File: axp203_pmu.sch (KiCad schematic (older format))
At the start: 1 part

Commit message: Updated PCB
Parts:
- U1: renamed from U?; footprint (none) -> X_Powers:AXP203_QFN48
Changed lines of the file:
@@
 $EndDescr
 $Comp
-L x_powers:AXP203 U?
+L x_powers:AXP203 U1
 U 1 1 5E09CC8E
 P 7900 5000
-F 0 "U?" H 7900 7565 50  0000 C CNN
+F 0 "U1" H 7900 7565 50  0000 C CNN
 F 1 "AXP203" H 7900 7474 50  0000 C CNN
-F 2 "" H 3550 7200 50  0001 C CNN
+F 2 "X_Powers:AXP203_QFN48" H 3550 7200 50  0001 C CNN
 F 3 "/home/mw/kicad_library/Schematic/PMU_Units/X_Powers/Components_Documentation/AXP203_Datasheet_V1.0.pdf" H 3550 7200 50  0001 C CNN
 	1    7900 5000

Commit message: Continue activity
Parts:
- removed U1: AXP203, X_Powers:AXP203_QFN48, symbol x_powers:AXP203
- added U?: AXP203, symbol x_powers:AXP203
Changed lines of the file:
@@
 $EndDescr
 $Comp
-L x_powers:AXP203 U1
-U 1 1 5E09CC8E
-P 7900 5000
-F 0 "U1" H 7900 7565 50  0000 C CNN
-F 1 "AXP203" H 7900 7474 50  0000 C CNN
-F 2 "X_Powers:AXP203_QFN48" H 3550 7200 50  0001 C CNN
-F 3 "/home/mw/kicad_library/Schematic/PMU_Units/X_Powers/Components_Documentation/AXP203_Datasheet_V1.0.pdf" H 3550 7200 50  0001 C CNN
-	1    7900 5000
+L x_powers:AXP203 U?
+U 1 1 5E04BBCA
+P 8350 5350
+F 0 "U?" H 8350 7915 50  0000 C CNN
+F 1 "AXP203" H 8350 7824 50  0000 C CNN
+F 2 "" H 4000 7550 50  0001 C CNN
+F 3 "/home/mw/kicad_library/Schematic/PMU_Units/X_Powers/Components_Documentation/AXP203_Datasheet_V1.0.pdf" H 4000 7550 50  0001 C CNN
+	1    8350 5350
 	1    0    0    -1
 $EndComp

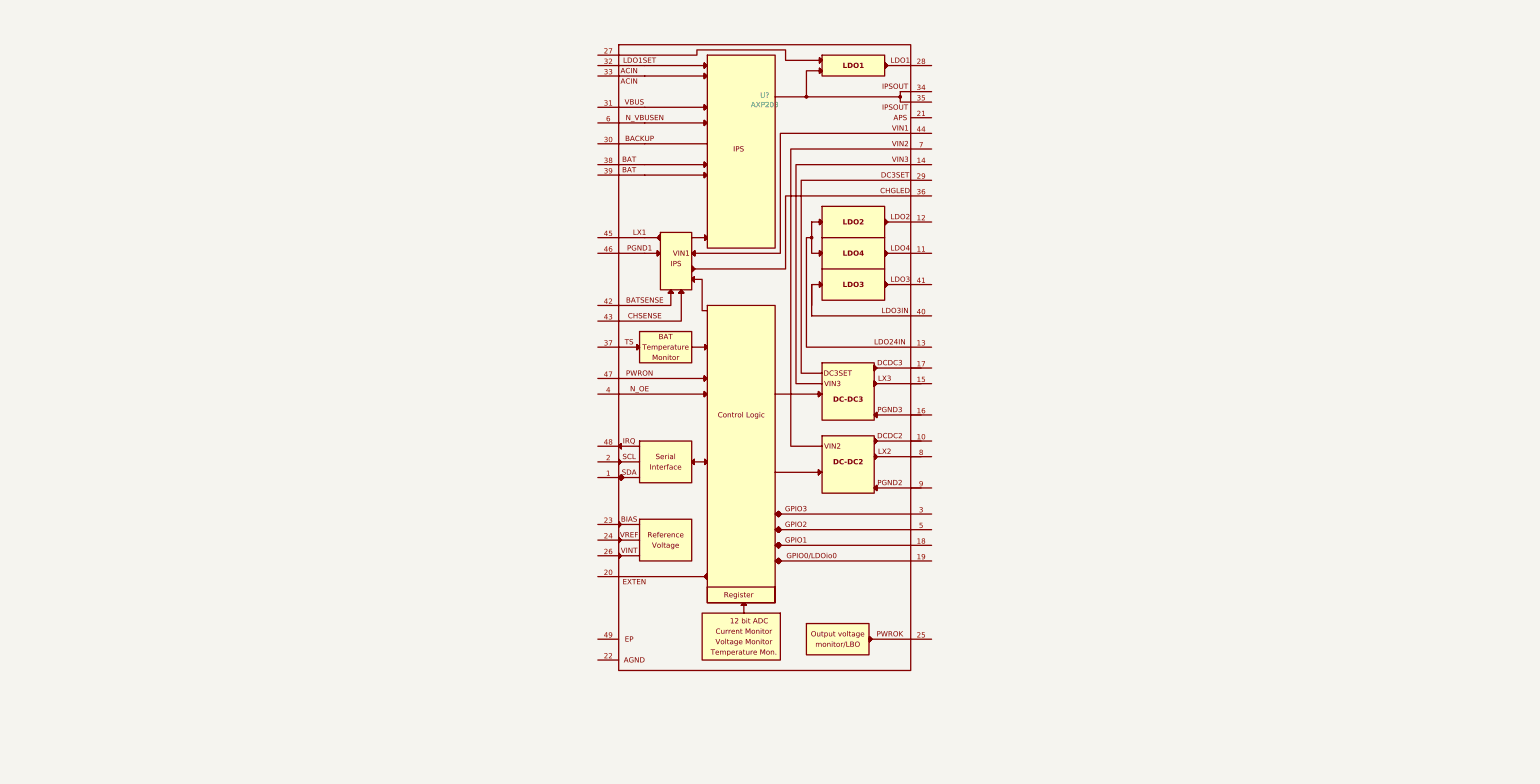
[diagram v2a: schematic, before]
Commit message: Schematic finished, pcb components added in pcb, axp schematic checked
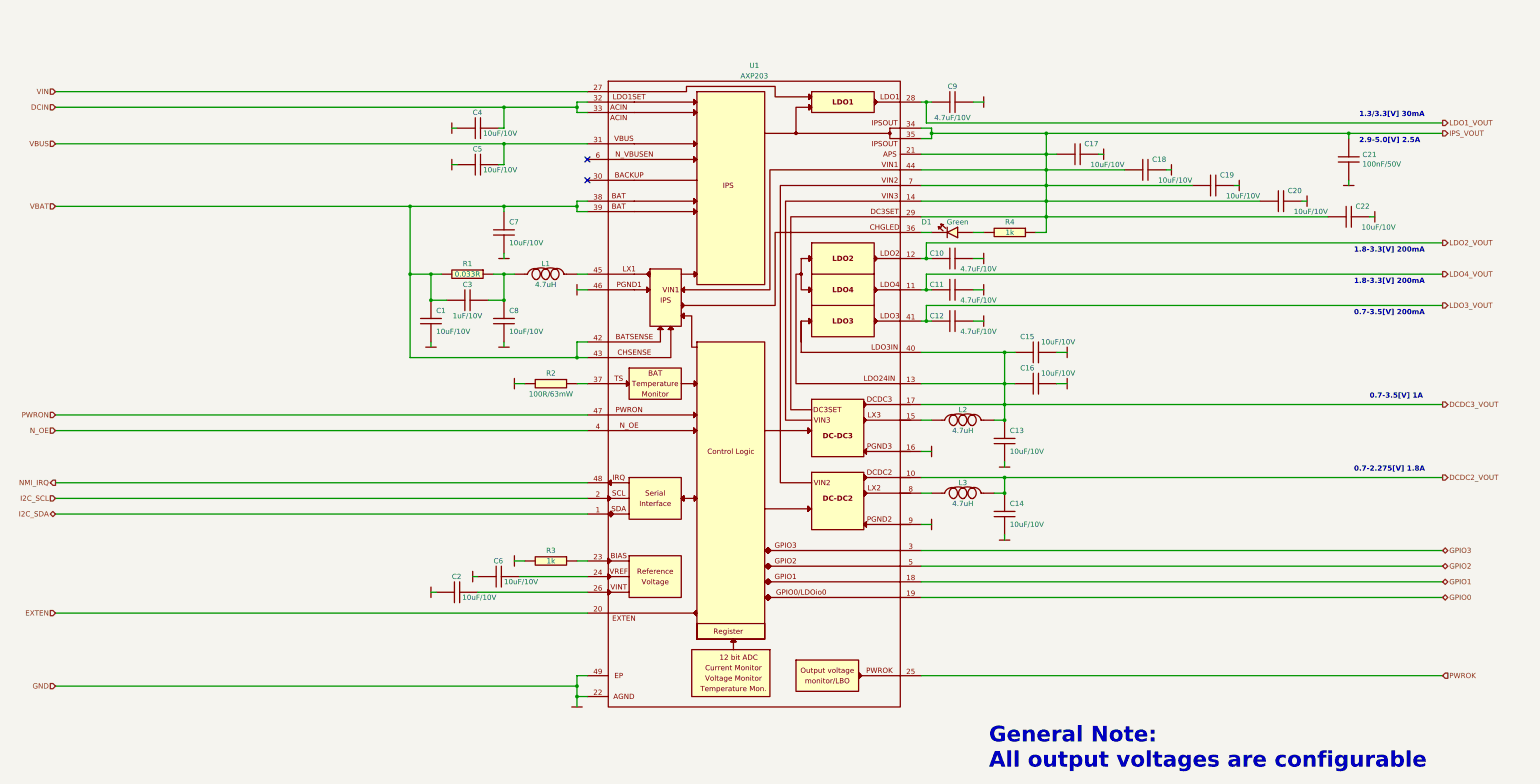
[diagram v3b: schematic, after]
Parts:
- added C1, C13, C14, C15, C16, C17, C18, C19, C2, C20, C22, C4, C5, C6, C7, C8: 10uF/10V, Capacitors_Smd_0603:10uF_10V_0603, symbol Capacitors_Smd0603:10uF_0603
- added C10, C11, C12, C9: 4.7uF/10V, Capacitors_Smd_0603:4_7uF_0603, symbol Capacitors_Smd0603:4_7uF_0603
- added C21: 100nF/50V, Capacitors_Smd_0603:100nF_0603, symbol Capacitors_Smd0603:100nF_0603
- added C3: 1uF/10V, Capacitors_Smd_0603:1uF_0603, symbol Capacitors_Smd0603:1uF_0603
- added D1: Green, Diodes:LED_KPT-1608CGCK, symbol Diodes:KPT-1608CGCK
- added L1, L2, L3: 4.7uH, Inductors:IHLP2020BZER4R7M01, symbol Inductors:IHLP2020BZER4R7M01
- added R1: 0.033R, Resistor_Smd_0603:0R033_0603, symbol Resistors_Smd0603:0.033R_0603
- added R2: 100R/63mW, Resistor_Smd_0603:100R_0603, symbol Resistors_Smd0603:100R_0603
- added R3, R4: 1k, Resistor_Smd_0603:1k_0603, symbol Resistors_Smd0603:1k_0603
- U1: renamed from U?; footprint (none) -> X_Powers:AXP203_QFN48
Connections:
- net I2C_SDA: now reaches U1.1 (SDA)
- net DCDC2_VOUT: now reaches U1.10 (DCDC2)
- net DCDC2_VOUT: now also C14.1, L3.2
- net LDO4_VOUT: now reaches U1.11 (LDO4)
- net LDO4_VOUT: now also C11.2
- net LDO2_VOUT: now reaches U1.12 (LDO2)
- net LDO2_VOUT: now also C10.2
- net DCDC3_VOUT: now reaches U1.13 (LDO24IN)
- net DCDC3_VOUT: now also U1.17 (DCDC3), U1.40 (LDO3IN), C13.1, C15.2, C16.2, L2.2
- net IPS_VOUT: now reaches U1.14 (VIN3)
- net IPS_VOUT: now also U1.21 (APS), U1.29 (DC3SET), U1.34 (IPSOUT), U1.35 (IPSOUT), U1.44 (VIN1), U1.7 (VIN2), C17.1, C18.1, C19.1, C20.1, C21.1, C22.1, R4.1
- net at U1.15 (LX3): now also L2.1
- net GND: now reaches U1.16 (PGND3)
- net GND: now also U1.22 (AGND), U1.46 (PGND1), U1.49 (EP), U1.9 (PGND2), C1.2, C10.1, C11.1, C12.1, C13.2, C14.2, C15.1, C16.1, C17.2, C18.2, C19.2, C2.2, C20.2, C21.2, C22.2, C4.2, C5.2, C6.2, C7.2, C8.2, C9.1, R2.2, R3.2
- net GPIO1: now reaches U1.18 (GPIO1)
- net GPIO0: now reaches U1.19 (GPIO0/LDOio0)
- net I2C_SCL: now reaches U1.2 (SCK)
- net EXTEN: now reaches U1.20 (EXTEN)
- net at U1.23 (BIAS): now also R3.1
- net at U1.24 (VREF): now also C6.1
- net PWROK: now reaches U1.25 (PWROK)
- net at U1.26 (VINT): now also C2.1
- net VIN: now reaches U1.27 (LDO1SET)
- net LDO1_VOUT: now reaches U1.28 (LDO1)
- net LDO1_VOUT: now also C9.2
- net GPIO3: now reaches U1.3 (GPIO3)
- net VBUS: now reaches U1.31 (VBUS)
- net VBUS: now also C5.1
- net DCIN: now reaches U1.32 (ACIN)
- net DCIN: now also U1.33 (ACIN), C4.1
- net at U1.36 (CHGLED): now also D1.2 (K)
- net at U1.37 (TS): now also R2.1
- net VBAT: now reaches U1.38 (BAT)
- net VBAT: now also U1.39 (BAT), U1.42 (BATSENSE), U1.43 (CHSENSE), C1.1, C3.2, C7.1, R1.2
- net N_OE: now reaches U1.4 (N_OE)
- net LDO3_VOUT: now reaches U1.41 (LDO3)
- net LDO3_VOUT: now also C12.2
- net at U1.45 (LX1): now also L1.2
- net PWRON: now reaches U1.47 (PWRON)
- net NMI_IRQ: now reaches U1.48 (IRQ)
- net GPIO2: now reaches U1.5 (GPIO2)
- net at U1.8 (LX2): now also L3.1
- new net: C3.1, C8.1, L1.1, R1.1
- new net: D1.1 (A), R4.2
- no-connect marks 0 -> 2
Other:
- note added: "0.7-2.275[V] 1.8A"
- note added: "0.7-3.5[V] 1A"
- note added: "0.7-3.5[V] 200mA"
- note added: "1.3/3.3[V] 30mA"
- note added: "1.8-3.3[V] 200mA"
- note added: "2.9-5.0[V] 2.5A"
- note added: "General Note:\nAll output voltages are configurable"
- moved on the sheet: U1
